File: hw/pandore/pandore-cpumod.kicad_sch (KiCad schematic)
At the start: 3 parts, among them U1 LattePanda_Mu

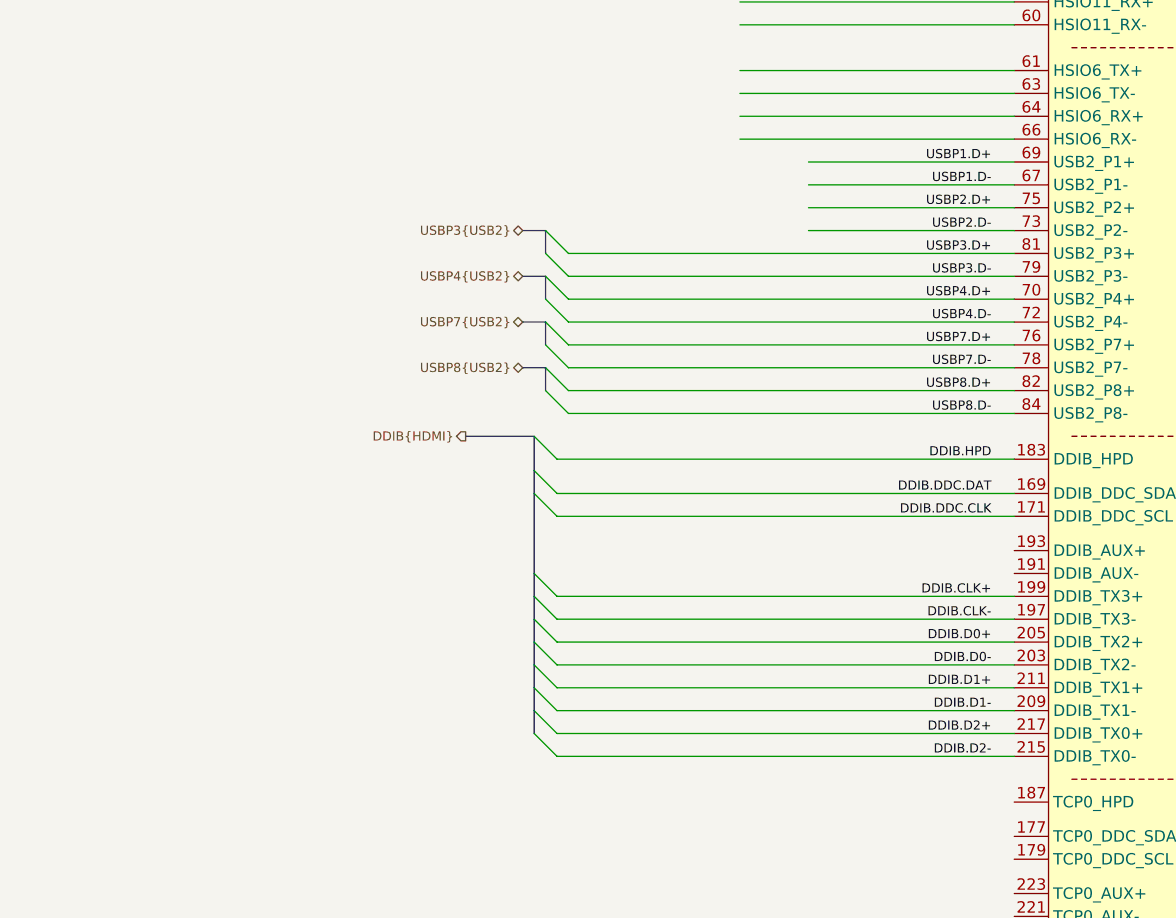
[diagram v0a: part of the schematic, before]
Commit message: added usb, hdmi and combo xlrtrs connectors resized pcb for something realistic (still wip)
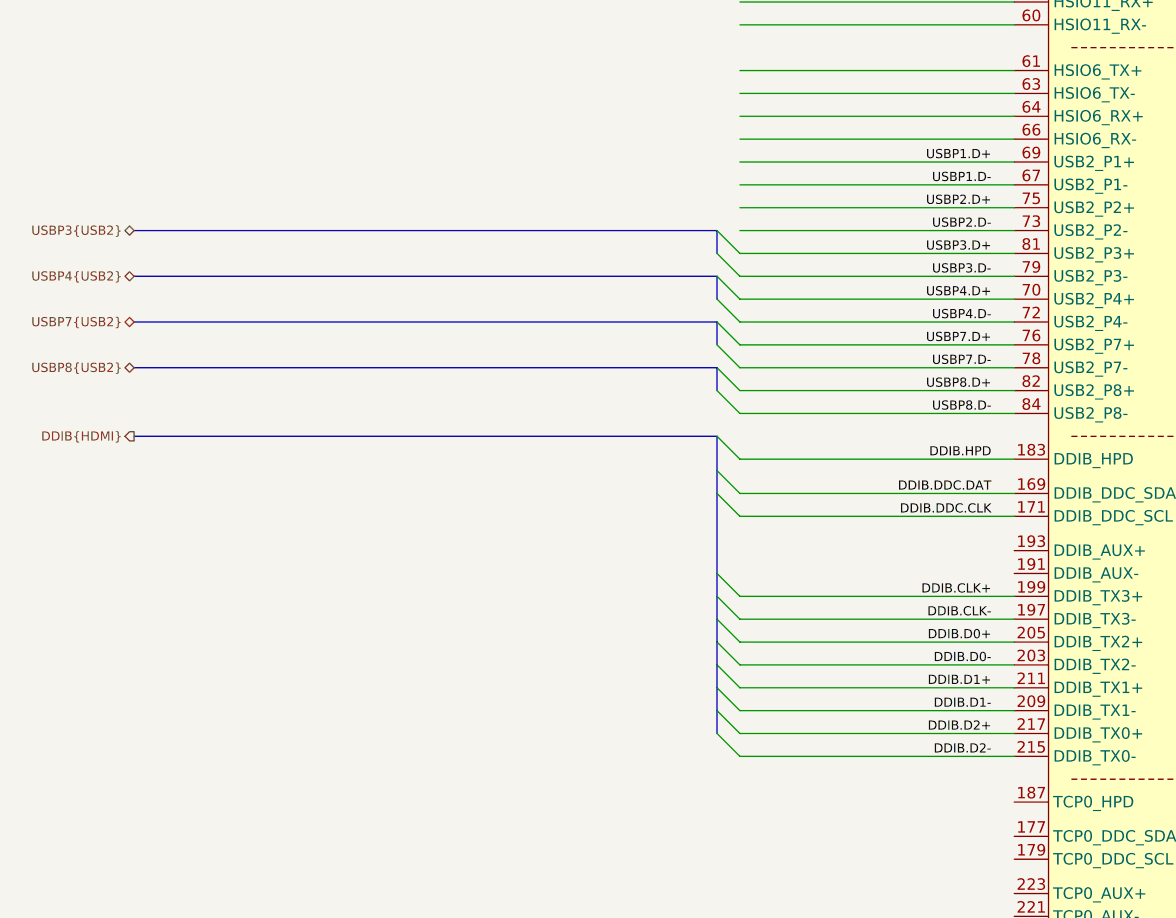
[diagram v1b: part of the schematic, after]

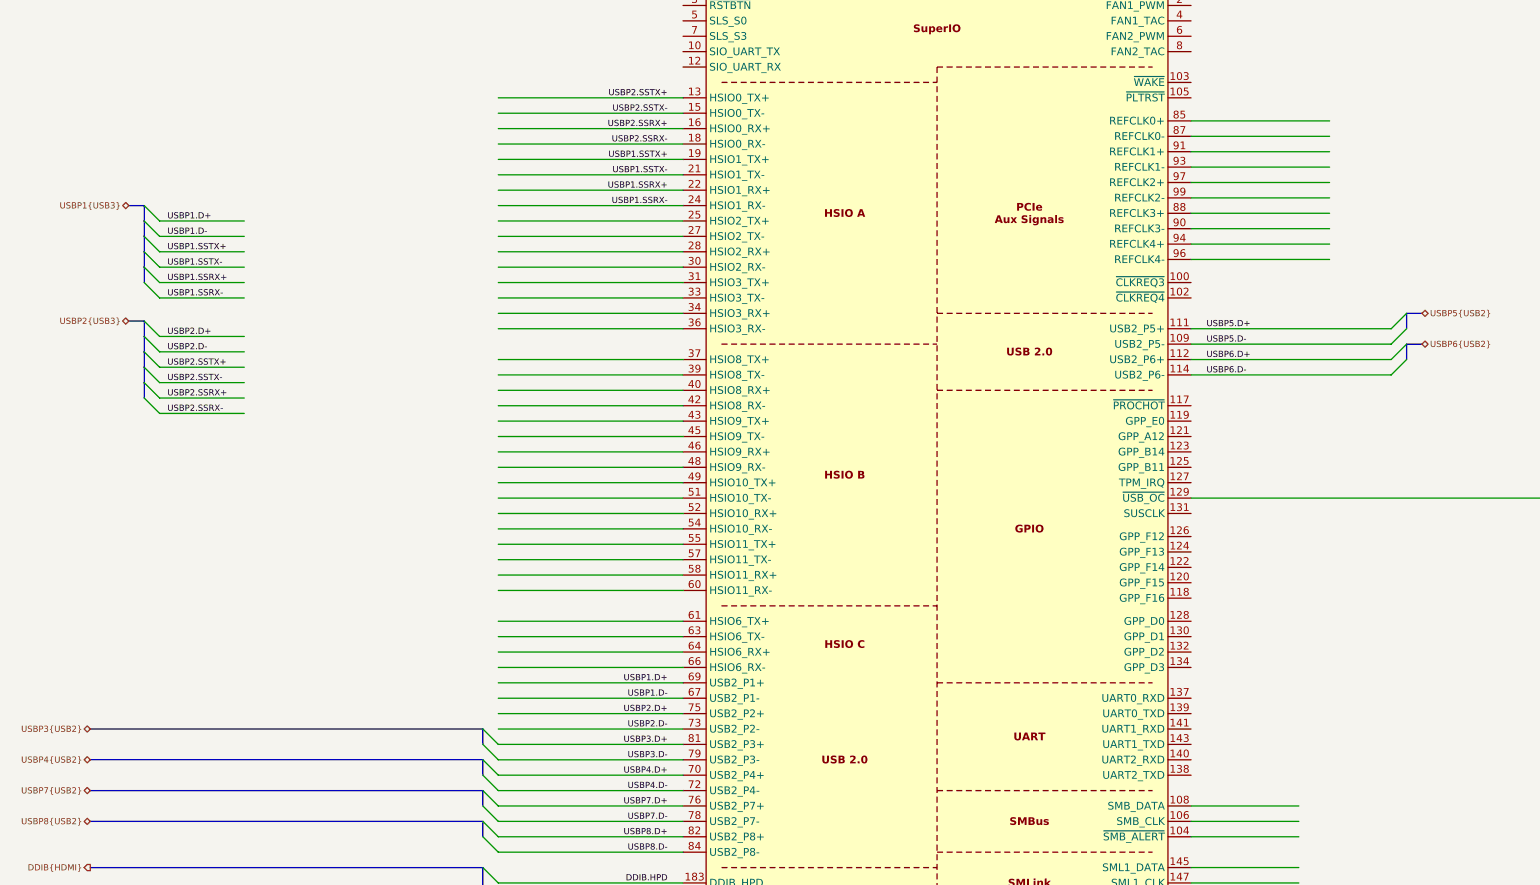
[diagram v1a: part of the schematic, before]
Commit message: Added lots to sch and pcb: eth passive, audio codec, midi, teensy Corrected and added support for M.2
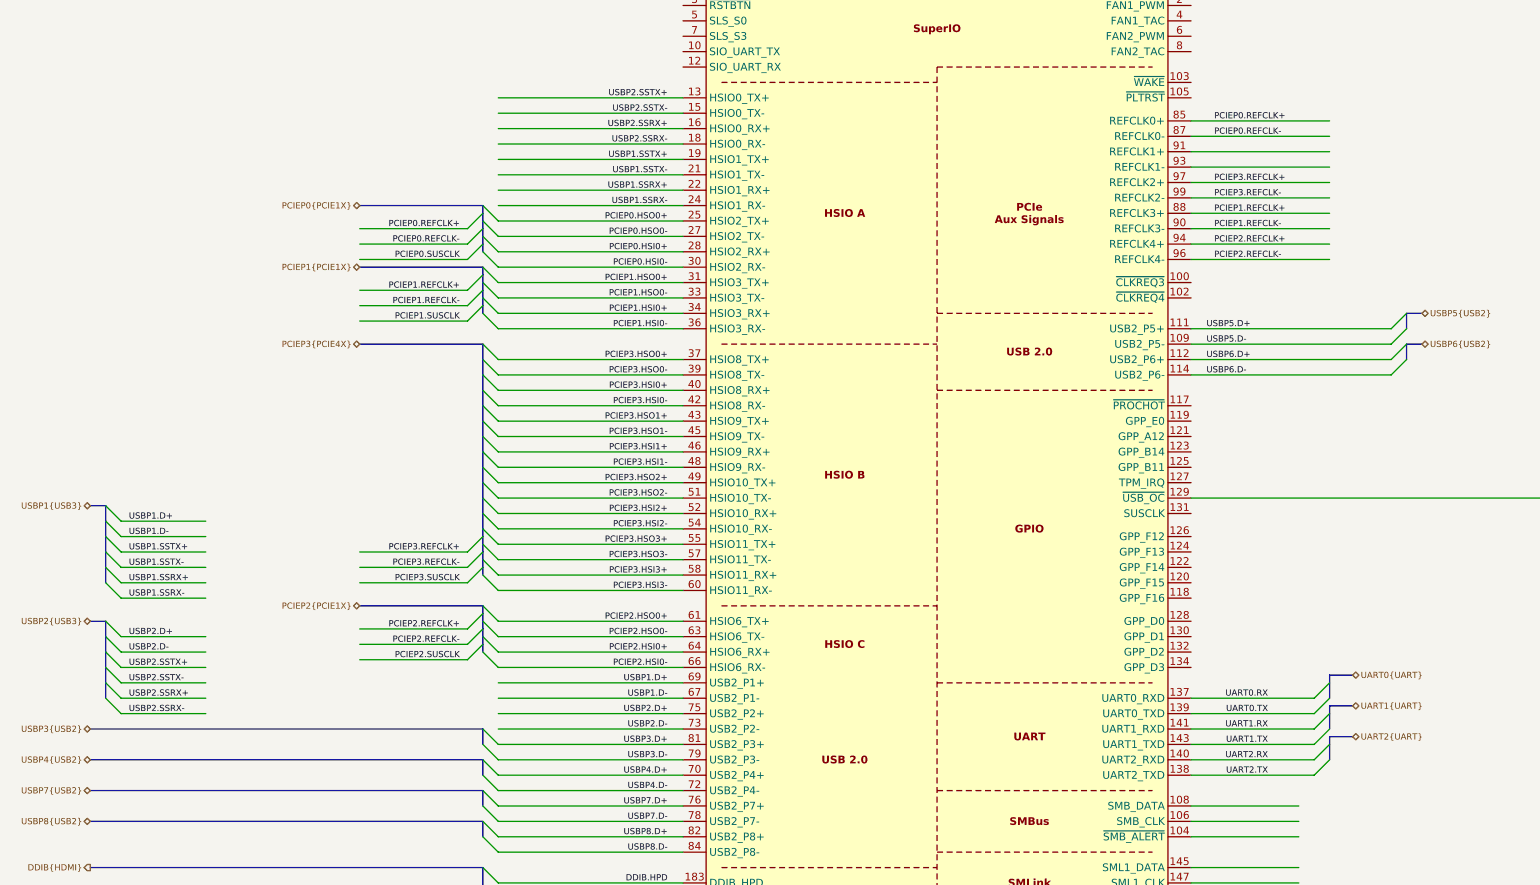
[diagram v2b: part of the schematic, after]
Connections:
- net UART0.RX: now reaches U1.137 (UART0_RXD)
- net UART2.TX: now reaches U1.138 (UART2_TXD)
- net UART0.TX: now reaches U1.139 (UART0_TXD)
- net UART2.RX: now reaches U1.140 (UART2_RXD)
- net UART1.RX: now reaches U1.141 (UART1_RXD)
- net UART1.TX: now reaches U1.143 (UART1_TXD)
- net PCIEP0.HSO0+: now reaches U1.25 (HSIO2_TX+)
- net PCIEP0.HSO0-: now reaches U1.27 (HSIO2_TX-)
- net PCIEP0.HSI0+: now reaches U1.28 (HSIO2_RX+)
- net PCIEP0.HSI0-: now reaches U1.30 (HSIO2_RX-)
- net PCIEP1.HSO0+: now reaches U1.31 (HSIO3_TX+)
- net PCIEP1.HSO0-: now reaches U1.33 (HSIO3_TX-)
- net PCIEP1.HSI0+: now reaches U1.34 (HSIO3_RX+)
- net PCIEP1.HSI0-: now reaches U1.36 (HSIO3_RX-)
- net PCIEP3.HSO0+: now reaches U1.37 (HSIO8_TX+)
- net PCIEP3.HSO0-: now reaches U1.39 (HSIO8_TX-)
- net PCIEP3.HSI0+: now reaches U1.40 (HSIO8_RX+)
- net PCIEP3.HSI0-: now reaches U1.42 (HSIO8_RX-)
- net PCIEP3.HSO1+: now reaches U1.43 (HSIO9_TX+)
- net PCIEP3.HSO1-: now reaches U1.45 (HSIO9_TX-)
- net PCIEP3.HSI1+: now reaches U1.46 (HSIO9_RX+)
- net PCIEP3.HSI1-: now reaches U1.48 (HSIO9_RX-)
- net PCIEP3.HSO2+: now reaches U1.49 (HSIO10_TX+)
- net PCIEP3.HSO2-: now reaches U1.51 (HSIO10_TX-)
- net PCIEP3.HSI2+: now reaches U1.52 (HSIO10_RX+)
- net PCIEP3.HSI2-: now reaches U1.54 (HSIO10_RX-)
- net PCIEP3.HSO3+: now reaches U1.55 (HSIO11_TX+)
- net PCIEP3.HSO3-: now reaches U1.57 (HSIO11_TX-)
- net PCIEP3.HSI3+: now reaches U1.58 (HSIO11_RX+)
- net PCIEP3.HSI3-: now reaches U1.60 (HSIO11_RX-)
- net PCIEP2.HSO0+: now reaches U1.61 (HSIO6_TX+)
- net PCIEP2.HSO0-: now reaches U1.63 (HSIO6_TX-)
- net PCIEP2.HSI0+: now reaches U1.64 (HSIO6_RX+)
- net PCIEP2.HSI0-: now reaches U1.66 (HSIO6_RX-)
- net PCIEP0.REFCLK+: now reaches U1.85 (REFCLK0+)
- net PCIEP0.REFCLK-: now reaches U1.87 (REFCLK0-)
- net PCIEP1.REFCLK+: now reaches U1.88 (REFCLK3+)
- net PCIEP1.REFCLK-: now reaches U1.90 (REFCLK3-)
- net PCIEP2.REFCLK+: now reaches U1.94 (REFCLK4+)
- net PCIEP2.REFCLK-: now reaches U1.96 (REFCLK4-)
- net PCIEP3.REFCLK+: now reaches U1.97 (REFCLK2+)
- net PCIEP3.REFCLK-: now reaches U1.99 (REFCLK2-)

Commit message: added power stuff revised M.2 for higher model and added m.2 mounts added power tap terminals
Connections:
- net I2S.MCLK: now reaches U1.160 (I2S_MCLK)
- net I2S.TXCLK: now reaches U1.162 (I2S_SCLK)
- net I2S.TXFS: now reaches U1.164 (I2S_SFRM)
- net I2S.TXD0: now reaches U1.166 (I2S_TXD)
- net I2S.RXD0: now reaches U1.168 (I2S_RXD)
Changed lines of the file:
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@@
 	)
 	(bus_entry
+		(at 256.54 222.25)
+		(size -2.54 2.54)
+		(stroke
+			(width 0)
+			(type default)
+		)
+	)
+	(bus_entry
 		(at 104.14 120.65)
 		(size 2.54 2.54)
@@
 	)
 	(bus_entry
+		(at 256.54 217.17)
+		(size -2.54 2.54)
+		(stroke
+			(width 0)
+			(type default)
+		)
+	)
+	(bus_entry
 		(at 104.14 60.96)
 		(size -2.54 2.54)
@@
 	)
 	(bus_entry
+		(at 256.54 227.33)
+		(size -2.54 2.54)
+		(stroke
+			(width 0)
+			(type default)
+		)
+	)
+	(bus_entry
 		(at 41.91 130.81)
 		(size 2.54 2.54)
@@
 	)
 	(bus_entry
+		(at 256.54 219.71)
+		(size -2.54 2.54)
+		(stroke
+			(width 0)
+			(type default)
+		)
+	)
+	(bus_entry
 		(at 41.91 135.89)
 		(size 2.54 2.54)
@@
 	)
 	(bus_entry
+		(at 256.54 224.79)
+		(size -2.54 2.54)
+		(stroke
+			(width 0)
+			(type default)
+		)
+	)
+	(bus_entry
 		(at 104.14 77.47)
 		(size 2.54 2.54)
@@
 	(bus
 		(pts
+			(xy 256.54 224.79) (xy 256.54 227.33)
+		)
+		(stroke
+			(width 0)
+			(type default)
+		)
+	)
+	(bus
+		(pts
 			(xy 243.84 137.16) (xy 243.84 138.43)
 		)
@@
 	(bus
 		(pts
+			(xy 256.54 222.25) (xy 256.54 224.79)
+		)
+		(stroke
+			(width 0)
+			(type default)
+		)
+	)
+	(bus
+		(pts
 			(xy 104.14 58.42) (xy 104.14 59.69)
 		)
@@
 	(bus
 		(pts
+			(xy 256.54 217.17) (xy 256.54 219.71)
+		)
+		(stroke
+			(width 0)
+			(type default)
+		)
+	)
+	(bus
+		(pts
 			(xy 104.14 191.77) (xy 104.14 194.31)
 		)
@@
 		)
 	)
+	(bus
+		(pts
+			(xy 256.54 219.71) (xy 256.54 222.25)
+		)
+		(stroke
+			(width 0)
+			(type default)
+		)
+	)
 	(wire
 		(pts
@@
 	(wire
 		(pts
+			(xy 220.98 229.87) (xy 254 229.87)
+		)
+		(stroke
+			(width 0)
+			(type default)
+		)
+	)
+	(wire
+		(pts
 			(xy 106.68 148.59) (xy 137.16 148.59)
 		)
@@
 		)
 	)
+	(wire
+		(pts
+			(xy 220.98 219.71) (xy 254 219.71)
+		)
+		(stroke
+			(width 0)
+			(type default)
+		)
+	)
 	(bus
 		(pts
@@
 	(wire
 		(pts
+			(xy 220.98 224.79) (xy 254 224.79)
+		)
+		(stroke
+			(width 0)
+			(type default)
+		)
+	)
+	(wire
+		(pts
 			(xy 220.98 148.59) (xy 241.3 148.59)
 		)
@@
 	(wire
 		(pts
+			(xy 220.98 222.25) (xy 254 222.25)
+		)
+		(stroke
+			(width 0)
+			(type default)
+		)
+	)
+	(wire
+		(pts
 			(xy 220.98 80.01) (xy 254 80.01)
 		)
@@
 	(bus
 		(pts
+			(xy 259.08 217.17) (xy 256.54 217.17)
+		)
+		(stroke
+			(width 0)
+			(type default)
+		)
+	)
+	(bus
+		(pts
 			(xy 104.14 67.31) (xy 104.14 68.58)
 		)
@@
 	(wire
 		(pts
+			(xy 220.98 227.33) (xy 254 227.33)
+		)
+		(stroke
+			(width 0)
+			(type default)
+		)
+	)
+	(wire
+		(pts
 			(xy 220.98 163.83) (xy 238.76 163.83)
 		)
@@
 		)
 	)
+	(label "I2S.TXD0"
+		(at 223.52 227.33 0)
+		(effects
+			(font
+				(size 1.016 1.016)
+			)
+			(justify left bottom)
+		)
+	)
 	(label "DDIB.D0-"
 		(at 134.62 189.23 180)
@@
 		)
 	)
+	(label "I2S.MCLK"
+		(at 223.52 219.71 0)
+		(effects
+			(font
+				(size 1.016 1.016)
+			)
+			(justify left bottom)
+		)
+	)
 	(label "PCIEP2.HSI0-"
 		(at 134.62 130.81 180)
@@
 		)
 	)
+	(label "I2S.TXCLK"
+		(at 223.52 222.25 0)
+		(effects
+			(font
+				(size 1.016 1.016)
+			)
+			(justify left bottom)
+		)
+	)
 	(label "PCIEP3.HSI2-"
 		(at 134.62 107.95 180)
@@
 		)
 	)
+	(label "I2S.RXD0"
+		(at 223.52 229.87 0)
+		(effects
+			(font
+				(size 1.016 1.016)
+			)
+			(justify left bottom)
+		)
+	)
+	(label "I2S.TXFS"
+		(at 223.52 224.79 0)
+		(effects
+			(font
+				(size 1.016 1.016)
+			)
+			(justify left bottom)
+		)
+	)
 	(label "DDIB.DDC.CLK"
 		(at 134.62 172.72 180)
@@
 		)
 	)
+	(hierarchical_label "I2S{I2S1DPX}"
+		(shape bidirectional)
+		(at 259.08 217.17 0)
+		(effects
+			(font
+				(size 1.016 1.016)
+			)
+			(justify left)
+		)
+	)
 	(hierarchical_label "USBP6{USB2}"
 		(shape bidirectional)
@@
 		)
 	)
+	(rule_area
+		(polyline
+			(pts
+				(xy 222.2896 217.17) (xy 233.7196 217.17) (xy 233.7196 233.68) (xy 222.2896 233.68)
+			)
+			(stroke
+				(width 0)
+				(type dash)
+			)
+			(fill
+				(type none)
+			)
+		)
+	)
 	(netclass_flag ""
 		(length 1.27)
@@
 			(effects
 				(font
+					(size 1.27 1.27)
+					(italic yes)
+				)
+			)
+		)
+	)
+	(netclass_flag ""
+		(length 1.27)
+		(shape diamond)
+		(at 233.7196 218.44 270)
+		(effects
+			(font
+				(size 1.016 1.016)
+			)
+			(justify right bottom)
+		)
+		(property "Netclass" "I2S"
+			(at 235.6246 218.44 0)
+			(effects
+				(font
+					(size 1.27 1.27)
+				)
+				(justify left)
+			)
+		)
+		(property "Component Class" ""
+			(at 47.0296 46.99 0)
+			(effects
+				(font

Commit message: added i2s/i2c isolation for audio section
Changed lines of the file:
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@@
 	)
 	(bus_entry
+		(at 256.54 229.87)
+		(size -2.54 2.54)
+		(stroke
+			(width 0)
+			(type default)
+		)
+	)
+	(bus_entry
 		(at 104.14 146.05)
 		(size 2.54 2.54)
@@
 	(bus
 		(pts
+			(xy 256.54 227.33) (xy 256.54 229.87)
+		)
+		(stroke
+			(width 0)
+			(type default)
+		)
+	)
+	(bus
+		(pts
 			(xy 83.82 64.77) (xy 104.14 64.77)
 		)
@@
 	(wire
 		(pts
+			(xy 242.57 232.41) (xy 254 232.41)
+		)
+		(stroke
+			(width 0)
+			(type default)
+		)
+	)
+	(wire
+		(pts
 			(xy 220.98 74.93) (xy 254 74.93)
 		)
@@
 		)
 	)
+	(label "I2S.~{RST}"
+		(at 245.11 232.41 0)
+		(effects
+			(font
+				(size 1.016 1.016)
+			)
+			(justify left bottom)
+		)
+	)
 	(label "USBP1.SSRX+"
 		(at 45.72 116.84 0)
@@
 		)
 	)
+	(label "I2S.~{RST}"
+		(at 234.95 109.22 0)
+		(effects
+			(font
+				(size 1.016 1.016)
+			)
+			(justify left bottom)
+		)
+	)
 	(label "USBP7.D-"
 		(at 134.62 156.21 180)
@@
 		)
 	)
-	(hierarchical_label "I2S{I2S1DPX}"
+	(hierarchical_label "I2S{I2S1DPX ~{RST}}"
 		(shape bidirectional)
 		(at 259.08 217.17 0)

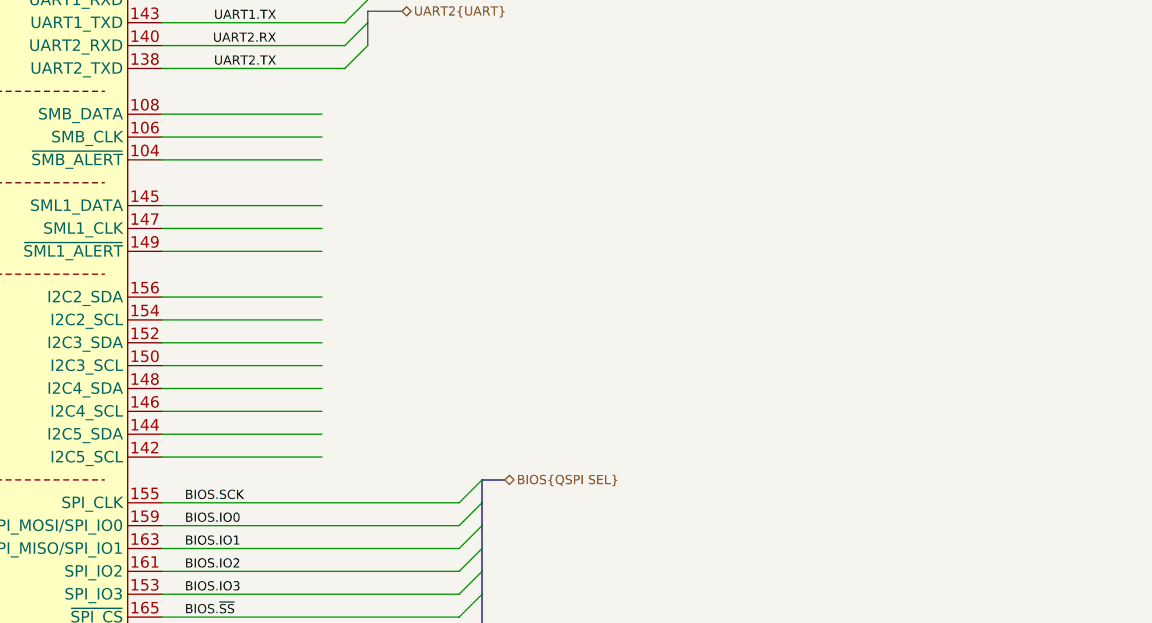
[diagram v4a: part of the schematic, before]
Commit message: lots of routing (diff, buses, power) done optimised buffer out
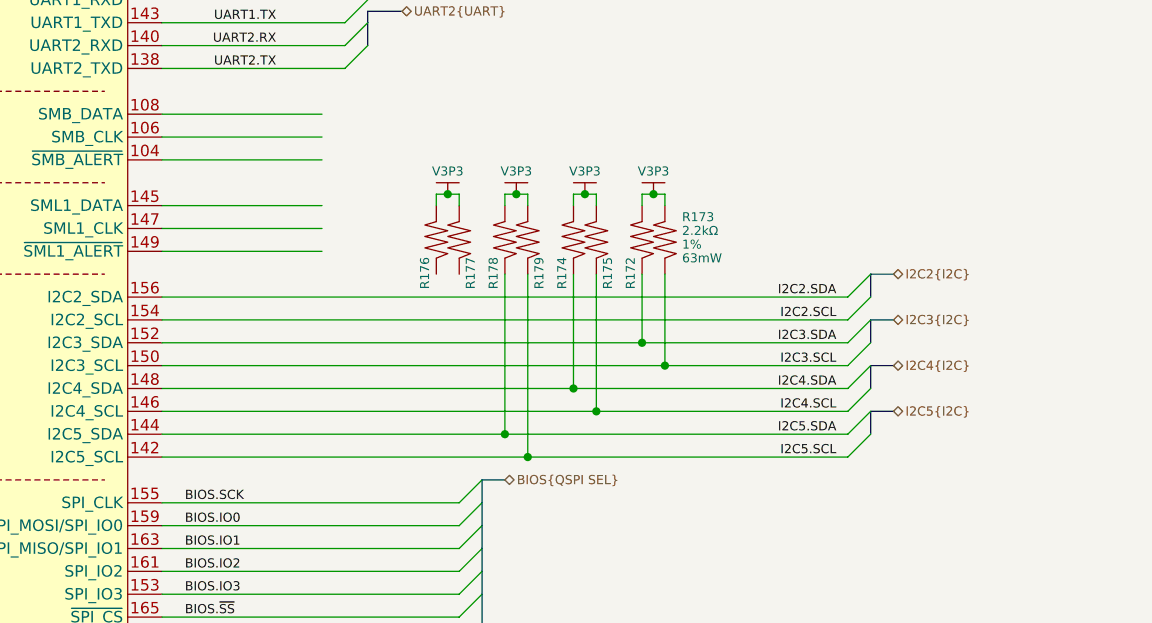
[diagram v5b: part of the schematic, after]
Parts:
- added R172, R173, R174, R175, R176, R177, R178, R179: ${Resistance}, ${Tolerance}, ${Power}, reekilib_res:RESC1005, symbol reekilib_res:res
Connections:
- net I2C5.SCL: now reaches U1.142 (I2C5_SCL)
- net I2C5.SCL: now also R179.2
- net I2C5.SDA: now reaches U1.144 (I2C5_SDA)
- net I2C5.SDA: now also R178.2
- net I2C4.SCL: now reaches U1.146 (I2C4_SCL)
- net I2C4.SCL: now also R175.2
- net I2C4.SDA: now reaches U1.148 (I2C4_SDA)
- net I2C4.SDA: now also R174.2
- net I2C3.SCL: now reaches U1.150 (I2C3_SCL)
- net I2C3.SCL: now also R173.2
- net I2C3.SDA: now reaches U1.152 (I2C3_SDA)
- net I2C3.SDA: now also R172.2
- net I2C2.SCL: now reaches U1.154 (I2C2_SCL)
- net I2C2.SDA: now reaches U1.156 (I2C2_SDA)
- new net V3P3: R172.1, R173.1, R174.1, R175.1, R176.1, R177.1, R178.1, R179.1
